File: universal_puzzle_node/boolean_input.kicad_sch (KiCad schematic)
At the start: 9 parts

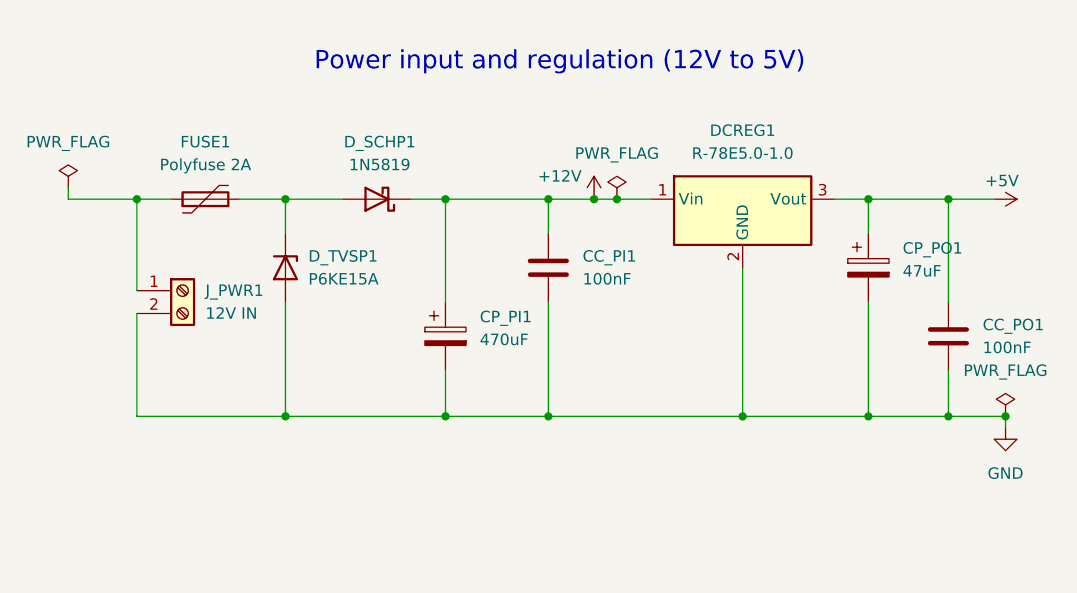
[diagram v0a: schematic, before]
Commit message: chore: rename to universal puzzle node everywhere
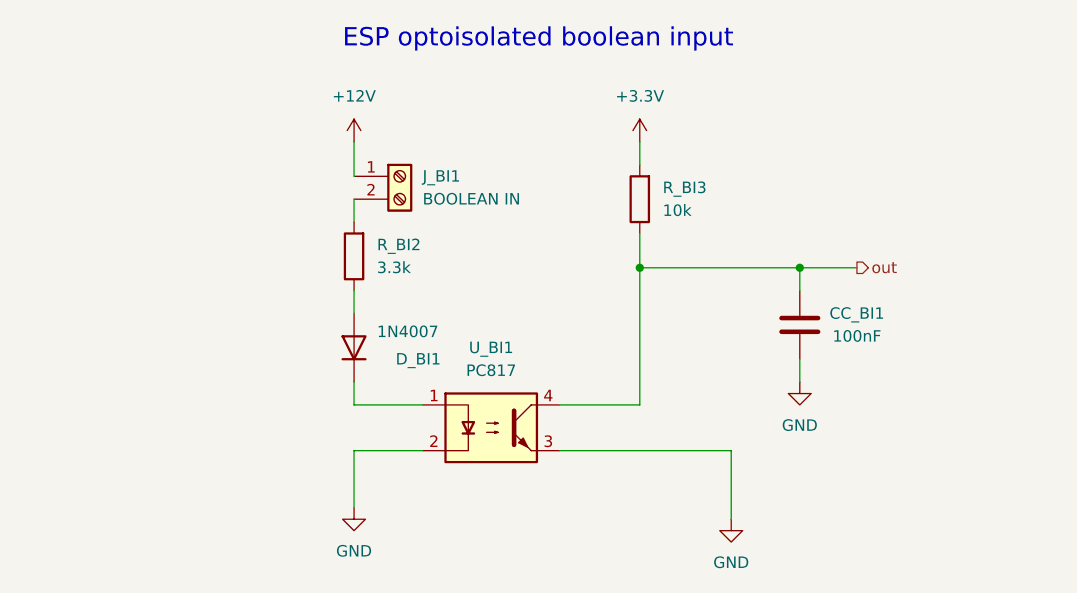
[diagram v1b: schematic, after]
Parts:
- removed CC_PI1, CC_PO1: 100nF, Capacitor_THT:C_Disc_D5.0mm_W2.5mm_P5.00mm, symbol Device:C
- removed CP_PI1: 470uF, Capacitor_THT:CP_Radial_D10.0mm_P5.00mm, symbol Device:C_Polarized
- removed CP_PO1: 47uF, Capacitor_THT:CP_Radial_D6.3mm_P2.50mm, symbol Device:C_Polarized
- removed DCREG1: R-78E5.0-1.0, Converter_DCDC:Converter_DCDC_RECOM_R-78E-0.5_THT, symbol Converter_DCDC:TSR2-2450
- removed D_SCHP1: 1N5819, Diode_THT:D_DO-35_SOD27_P7.62mm_Horizontal, symbol Device:D_Schottky
- removed D_TVSP1: P6KE15A, Diode_THT:D_DO-15_P12.70mm_Horizontal, symbol Diode:PTVS15VZ1USK
- removed FUSE1: Polyfuse 2A, Fuse:Fuse_BelFuse_0ZRE0040FF_L11.5mm_W3.8mm, symbol Device:Polyfuse
- removed J_PWR1: 12V IN, TerminalBlock_Phoenix:TerminalBlock_Phoenix_MKDS-1,5-2-5.08_1x02_P5.08mm_Horizontal, symbol Connector:Screw_Terminal_01x02
- added CC_BI1: 100nF, Capacitor_THT:C_Disc_D5.0mm_W2.5mm_P5.00mm, symbol Device:C
- added D_BI1: 1N4007, Diode_THT:D_DO-41_SOD81_P10.16mm_Horizontal, symbol Diode:1N4007
- added J_BI1: BOOLEAN IN, TerminalBlock_Phoenix:TerminalBlock_Phoenix_MKDS-1,5-2-5.08_1x02_P5.08mm_Horizontal, symbol Connector:Screw_Terminal_01x02
- added R_BI2: 3.3k, Resistor_THT:R_Axial_DIN0207_L6.3mm_D2.5mm_P10.16mm_Horizontal, symbol Device:R
- added R_BI3: 10k, Resistor_THT:R_Axial_DIN0207_L6.3mm_D2.5mm_P10.16mm_Horizontal, symbol Device:R
- added U_BI1: PC817, Package_DIP:DIP-4_W7.62mm, symbol Isolator:PC817
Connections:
- net +12V: now also J_BI1.1 (Pin_1)
- net GND: now also CC_BI1.2, U_BI1.2, U_BI1.3
- new net: D_BI1.1 (K), U_BI1.1
- new net: D_BI1.2 (A), R_BI2.1
- new net: J_BI1.2 (Pin_2), R_BI2.2
- new net +3.3V: R_BI3.2
- new net out: CC_BI1.1, R_BI3.1, U_BI1.4
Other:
- note added: "ESP optoisolated boolean input"
- note removed: "Power input and regulation (12V to 5V)"
- title: Power input and regulation -> ESP optoisolated boolean input
